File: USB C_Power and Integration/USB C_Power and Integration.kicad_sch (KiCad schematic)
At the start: 4 parts, among them J1 TYPE-C-31-M-08A, U1 TP4065-4.2V-SOT25-R, U2 BQ24074RGTR, U3 HUSB237-AA001-DN06R

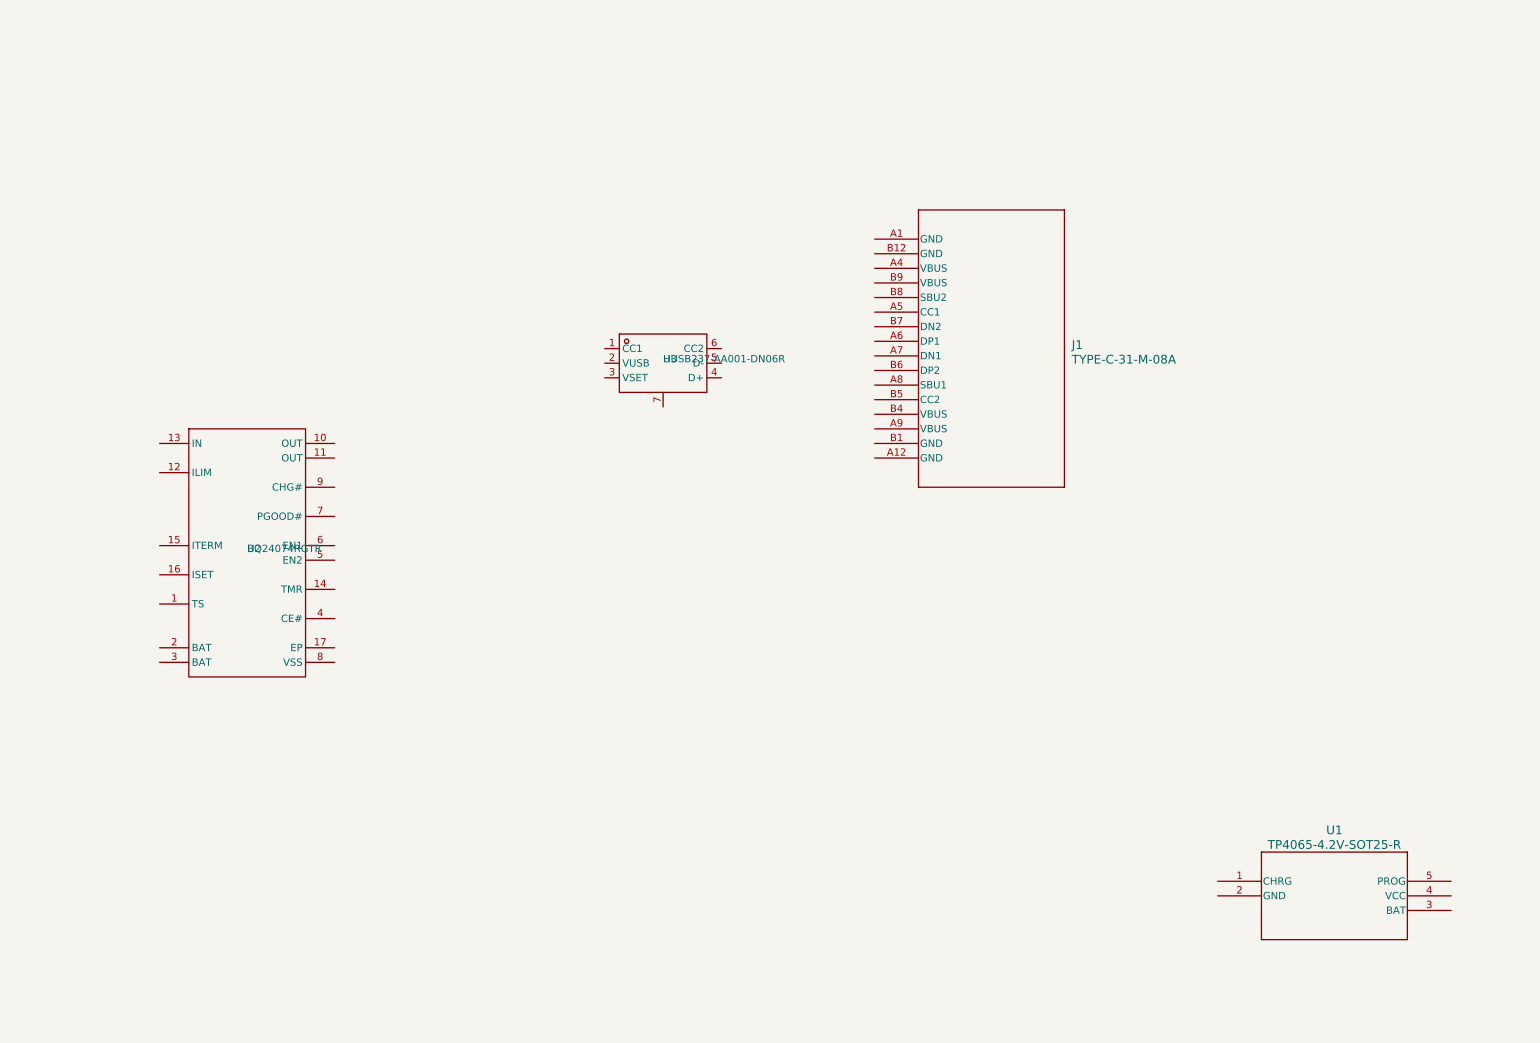
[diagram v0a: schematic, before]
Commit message: All MJ's requirements schematics done (review pending)
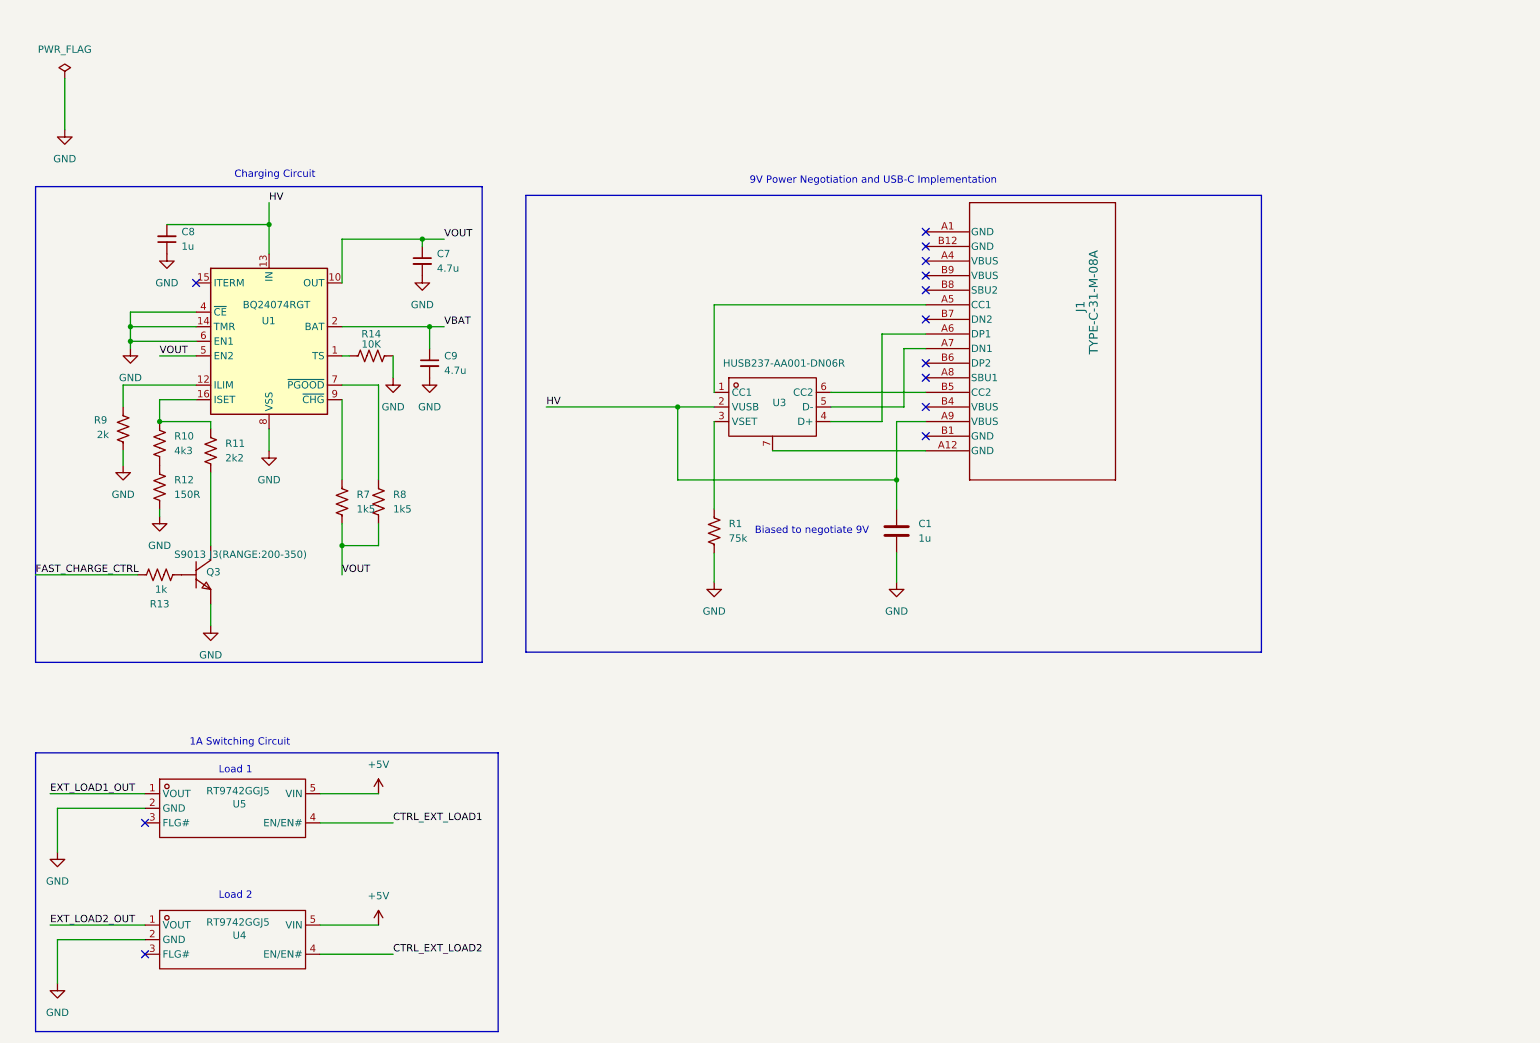
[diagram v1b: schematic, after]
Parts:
- removed U1: TP4065-4.2V-SOT25-R, SOT-23-5L_TPW, symbol TP4065-4.2V-SOT235:TP4065-4.2V-SOT25-R
- removed U2: BQ24074RGTR, QFN-16_L3.0-W3.0-P0.50-TL-EP1.7, symbol BQ24074RGTR1_BQ24074RGTR-altium-import:root_0_BQ24074RGTR_
- added C1: 1u, symbol Device:C
- added C7, C9: 4.7u, symbol Device:C_Small
- added C8: 1u, symbol Device:C_Small
- added Q3: S9013 J3(RANGE:200-350), SOT-23-3_L2.9-W1.3-P1.90-LS2.4-BR, symbol S9013 J31_S9013 J3-altium-import:root_0_S9013 J3(RANGE{colon}200-350)_
- added R1: 75k, symbol Device:R_US
- added R10: 4k3, symbol Device:R_US
- added R11: 2k2, symbol Device:R_US
- added R12: 150R, symbol Device:R_US
- added R13: 1k, symbol Device:R_US
- added R14: 10K, symbol Device:R_US
- added R7, R8: 1k5, symbol Device:R_US
- added R9: 2k, symbol Device:R_US
- added U1: BQ24074RGT, Package_DFN_QFN:VQFN-16-1EP_3x3mm_P0.5mm_EP1.6x1.6mm, symbol Battery_Management:BQ24074RGT
- added U4, U5: RT9742GGJ5, TSOT-23-5_L2.9-W1.6-P0.95-LS2.8-BR, symbol RT9742GGJ51_RT9742GGJ5-altium-import:root_0_RT9742GGJ5_
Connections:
- net at J1.A12 (GND): now also U3.7 (GND)
- net at J1.A5 (CC1): now also U3.1 (CC1)
- net at J1.A6 (DP1): now also U3.4 (D+)
- net at J1.A7 (DN1): now also U3.5 (D-)
- net HV: now reaches J1.A9 (VBUS)
- net HV: now also U3.2 (VUSB), C1.1, C8.2, U1.13 (IN)
- net at J1.B5 (CC2): now also U3.6 (CC2)
- net at U3.3 (VSET): now also R1.1
- new net: R14.1, U1.1 (TS)
- new net: Q3.1 (B), R13.2
- new net: R7.1, U1.9 (~{CHG})
- new net: R8.1, U1.7 (~{PGOOD})
- new net: R9.1, U1.12 (ILIM)
- new net: R10.1, R11.1, U1.16 (ISET)
- new net: Q3.3 (C), R11.2
- new net: R10.2, R12.1
- new net +5V: U4.5 (VIN), U5.5 (VIN)
- new net CTRL_EXT_LOAD1: U5.4 (EN/EN#)
- new net CTRL_EXT_LOAD2: U4.4 (EN/EN#)
- new net EXT_LOAD1_OUT: U5.1 (VOUT)
- new net EXT_LOAD2_OUT: U4.1 (VOUT)
- new net FAST_CHARGE_CTRL: R13.1
- new net GND: C1.2, C7.2, C8.1, C9.2, Q3.2 (E), R1.2, R12.2, R14.2, R9.2, U1.14 (TMR), U1.17 (VSS), U1.4 (~{CE}), U1.6 (EN1), U1.8 (VSS), U4.2 (GND), U5.2 (GND)
- new net VBAT: C9.1, U1.2 (BAT), U1.3 (BAT)
- new net VOUT: C7.1, R7.2, R8.2, U1.10 (OUT), U1.11 (OUT), U1.5 (EN2)
- no-connect marks 0 -> 13
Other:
- note added: "1A Switching Circuit"
- note added: "9V Power Negotiation and USB-C Implementation"
- note added: "Biased to negotiate 9V"
- note added: "Charging Circuit"
- note added: "Load 1"
- note added: "Load 2"
- moved on the sheet: J1, U3

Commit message: Polished USB C Power and Charging Integration and Switching Circuit with Footprints
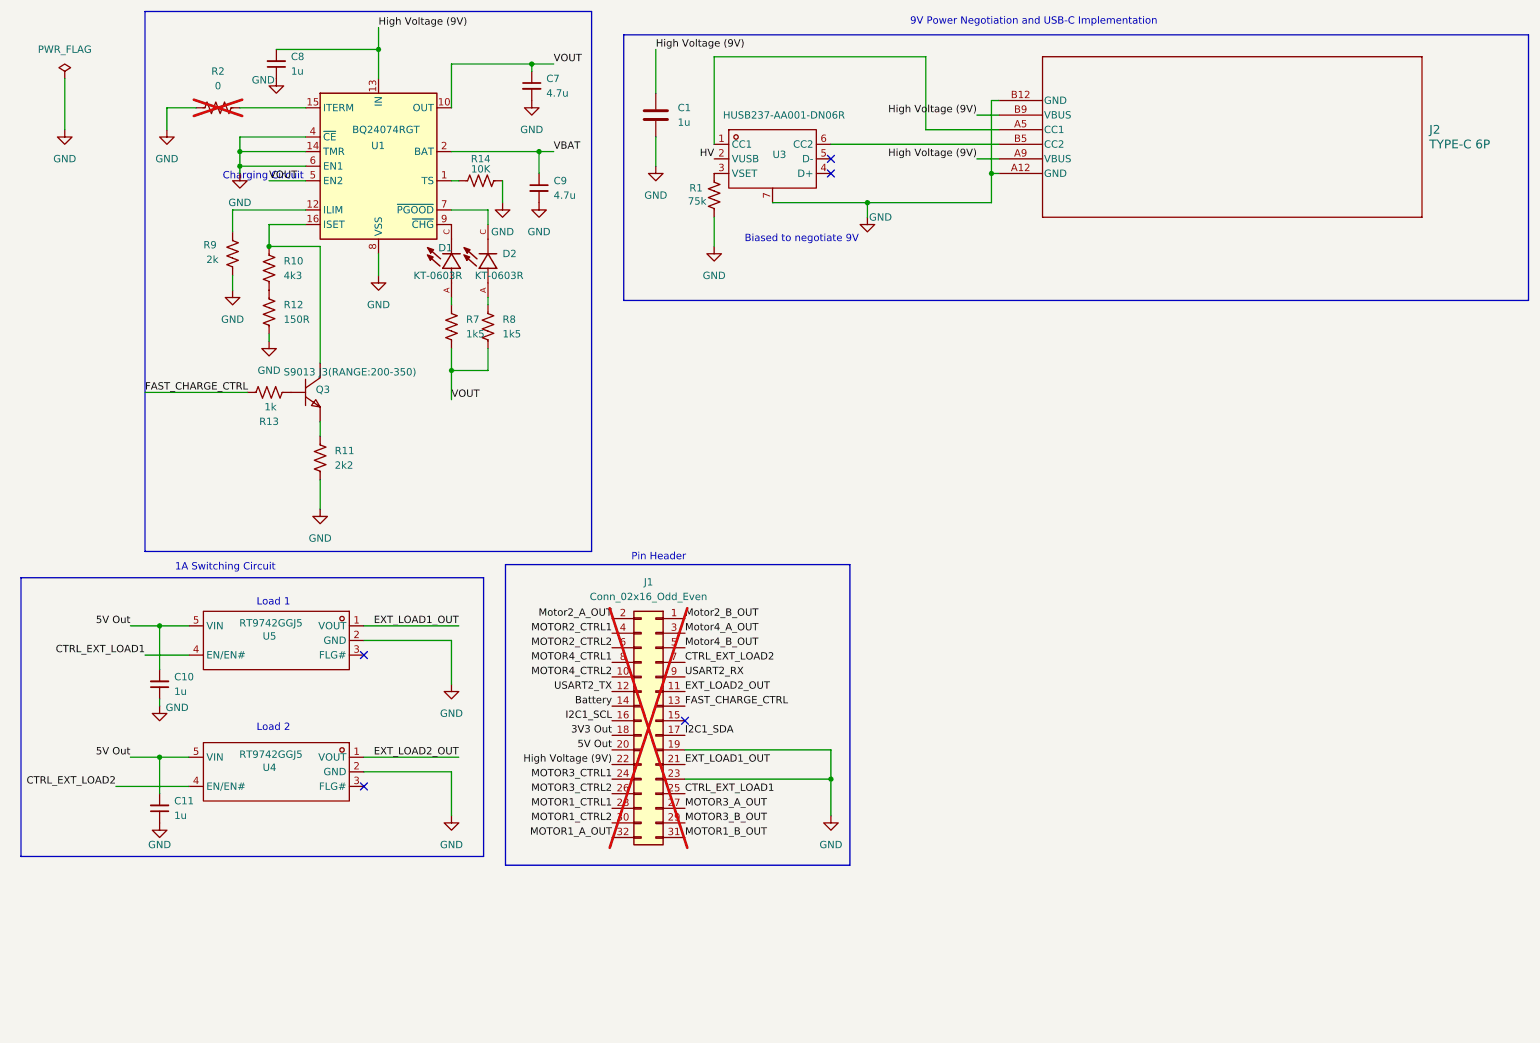
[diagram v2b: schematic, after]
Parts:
- removed J1: TYPE-C-31-M-08A, CONN16_1-M-08A_HRO, symbol TYPE-C-31-M-08A:TYPE-C-31-M-08A
- added C10, C11: 1u, Capacitor_SMD:C_1206_3216Metric_Pad1.33x1.80mm_HandSolder, symbol Device:C_Small
- added D1, D2: KT-0603R, KT-0603R:LED_KT-0603R, symbol KT-0603R:KT-0603R
- added J1: Conn_02x16_Odd_Even, Connector_PinHeader_2.54mm:PinHeader_2x16_P2.54mm_Vertical, symbol Connector_Generic:Conn_02x16_Odd_Even
- added J2: TYPE-C 6P, Connector_USB:USB_C_Receptacle_GCT_USB4125-xx-x_6P_TopMnt_Horizontal, symbol TYPE-C 6P(073):TYPE-C_6P
- added R2: 0, Resistor_SMD:R_0402_1005Metric_Pad0.72x0.64mm_HandSolder, symbol Device:R_US
- C1, C8: footprint (none) -> Capacitor_SMD:C_1206_3216Metric_Pad1.33x1.80mm_HandSolder
- C7: footprint (none) -> Capacitor_SMD:C_0402_1005Metric; LCSC C1779 -> C23733
- C9: footprint (none) -> Capacitor_SMD:C_0402_1005Metric_Pad0.74x0.62mm_HandSolder; LCSC C1779 -> C23733
- Q3: footprint SOT-23-3_L2.9-W1.3-P1.90-LS2.4-BR -> Package_TO_SOT_SMD:SOT-23_Handsoldering
- R1: footprint (none) -> Resistor_SMD:R_0603_1608Metric_Pad0.98x0.95mm_HandSolder
- R10: footprint (none) -> Resistor_SMD:R_0402_1005Metric_Pad0.72x0.64mm_HandSolder; LCSC C23159 -> C25899
- R11: footprint (none) -> Resistor_SMD:R_0402_1005Metric_Pad0.72x0.64mm_HandSolder; LCSC C4190 -> C25879
- R12: footprint (none) -> Resistor_SMD:R_0815_2038Metric_Pad1.20x4.05mm_HandSolder
- R13: footprint (none) -> Resistor_SMD:R_0402_1005Metric_Pad0.72x0.64mm_HandSolder; JCSC C4410 -> C11702
- R14: footprint (none) -> Resistor_SMD:R_0402_1005Metric_Pad0.72x0.64mm_HandSolder; LCSC C17414 -> C25744
- R7, R8: footprint (none) -> Resistor_SMD:R_0402_1005Metric_Pad0.72x0.64mm_HandSolder; LCSC C22843 -> C25867
- R9: footprint (none) -> Resistor_SMD:R_0402_1005Metric_Pad0.72x0.64mm_HandSolder
- U3: footprint TDFN-6_L2.0-W2.0-P0.65-TL-EP -> Package_DFN_QFN:DFN-6-1EP_2x2mm_P0.65mm_EP1.01x1.7mm
- U4, U5: footprint TSOT-23-5_L2.9-W1.6-P0.95-LS2.8-BR -> Package_TO_SOT_SMD:TSOT-23-5_HandSoldering
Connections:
- net CTRL_EXT_LOAD1: now also J1.25 (Pin_25)
- net CTRL_EXT_LOAD2: now also J1.7 (Pin_7)
- net EXT_LOAD1_OUT: now also J1.21 (Pin_21)
- net EXT_LOAD2_OUT: now also J1.11 (Pin_11)
- net FAST_CHARGE_CTRL: now also J1.13 (Pin_13)
- net GND: now also R11.2, U3.7 (GND), C10.1, C11.1, J1.19 (Pin_19), J1.23 (Pin_23), J2.A12 (GND), J2.B12 (GND), R2.1; no longer Q3.2 (E)
- net HV: no longer C1.1, C8.2, U1.13 (IN)
- net at R7.1: now also D1.A; no longer U1.9 (~{CHG})
- net at R8.1: now also D2.A; no longer U1.7 (~{PGOOD})
- net at U3.1 (CC1): now also J2.A5 (CC1)
- net at U3.6 (CC2): now also J2.B5 (CC2)
- net at U1.15 (ITERM): now also R2.2
- net at R10.1, U1.16 (ISET): now also Q3.3 (C); no longer R11.1
- net +5V renamed 5V Out
- net 5V Out: now also C10.2, C11.2, J1.20 (Pin_20)
- new net: D2.C, U1.7 (~{PGOOD})
- new net: D1.C, U1.9 (~{CHG})
- new net: Q3.2 (E), R11.1
- new net 3V3 Out: J1.18 (Pin_18)
- new net Battery: J1.14 (Pin_14)
- new net High Voltage (9V): C1.1, C8.2, J1.22 (Pin_22), J2.A9 (VBUS), J2.B9 (VBUS), U1.13 (IN)
- new net I2C1_SCL: J1.16 (Pin_16)
- new net I2C1_SDA: J1.17 (Pin_17)
- new net MOTOR1_A_OUT: J1.32 (Pin_32)
- new net MOTOR1_B_OUT: J1.31 (Pin_31)
- new net MOTOR1_CTRL1: J1.28 (Pin_28)
- new net MOTOR1_CTRL2: J1.30 (Pin_30)
- new net MOTOR2_CTRL1: J1.4 (Pin_4)
- new net MOTOR2_CTRL2: J1.6 (Pin_6)
- new net MOTOR3_A_OUT: J1.27 (Pin_27)
- new net MOTOR3_B_OUT: J1.29 (Pin_29)
- new net MOTOR3_CTRL1: J1.24 (Pin_24)
- new net MOTOR3_CTRL2: J1.26 (Pin_26)
- new net MOTOR4_CTRL1: J1.8 (Pin_8)
- new net MOTOR4_CTRL2: J1.10 (Pin_10)
- new net Motor2_A_OUT: J1.2 (Pin_2)
- new net Motor2_B_OUT: J1.1 (Pin_1)
- new net Motor4_A_OUT: J1.3 (Pin_3)
- new net Motor4_B_OUT: J1.5 (Pin_5)
- new net USART2_RX: J1.9 (Pin_9)
- new net USART2_TX: J1.12 (Pin_12)
- no-connect marks 13 -> 5
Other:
- note added: "Pin Header"
- moved on the sheet: C1, C7, C8, C9, Q3, R1, R10, R11, R12, R13, R14, R7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
